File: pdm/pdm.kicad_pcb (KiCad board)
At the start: 4 copper layers, 129.5 x 91.4 mm, 111 parts, among them J1 Conn_01x04_Male, J2 Conn_01x12_Male, J3 Conn_01x08_Male, Q1 MMBT3904, Q10 Q_NPN_BCE, Q2 Q_NPN_BCE, Q3 MMBT3904, Q4 Q_NPN_BCE, Q5 MMBT3904, Q6 Q_NPN_BCE, Q7 MMBT3904, Q8 Q_NPN_BCE, Q9 MMBT3904, SW1 SW_Push, U1 AZ1117CH-3_3TRG1, U2 SN65HVD233, U3 STM32F042G6Ux, U4 BTS443P, U5 BTS443P, U6 BTS443P, U7 BTS443P, U8 BTS443P

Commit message: fixed issues #7 #8 #9 #10
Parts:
- removed 3V3_TP1, GND_TP1, Vin_TP1: TestPoint_Probe, TestPoint:TestPoint_Pad_D1.0mm
- removed C11: 22uF, Capacitor_SMD:CP_Elec_6.3x5.8
- removed G***: LOGO, pdm_v2:rarepepe
- added C1: 1uF, Capacitor_SMD:C_0805_2012Metric_Pad1.18x1.45mm_HandSolder, F.Cu at (158.3, 84.9)
- added J4: Conn_01x06_Female, Connector_PinHeader_2.54mm:PinHeader_1x06_P2.54mm_Vertical_SMD_Pin1Left, F.Cu at (176.4, 59.7)
- added M1: Fan, Connector_JST:JST_EH_B2B-EH-A_1x02_P2.50mm_Vertical, F.Cu at (218.1, 115.3)
- added M2: Fan, Connector_JST:JST_EH_B2B-EH-A_1x02_P2.50mm_Vertical, F.Cu at (218.1, 124.5)
- added Q11: Q_PMOS_DSG, Package_TO_SOT_SMD:TO-252-2, F.Cu at (153.8, 122.8)
- added R4: 120R, Capacitor_SMD:C_0805_2012Metric_Pad1.18x1.45mm_HandSolder, F.Cu at (208.2, 69.2)
- added TP9: TestPoint_Probe, TestPoint:TestPoint_Pad_D1.0mm, F.Cu at (118.7, 66.0)
- C10, C7, C8: moved to F.Cu
- C12, C13, C14, C15: value 10uF -> 1uF; footprint Capacitor_Tantalum_SMD:CP_EIA-3216-18_Kemet-A_Pad1.58x1.35mm_HandSolder -> Capacitor_SMD:C_0805_2012Metric_Pad1.18x1.45mm_HandSolder
- C16: value 10uF -> 0.1uF; footprint Capacitor_Tantalum_SMD:CP_EIA-3216-18_Kemet-A_Pad1.58x1.35mm_HandSolder -> Capacitor_SMD:C_0805_2012Metric_Pad1.18x1.45mm_HandSolder
- C3: value 0.1uF -> 0.1u
- C4, C5: value 20pF -> 16pF
- C6: value 10uF -> 10u
- H1, H2, H3, H4: footprint MountingHole:MountingHole_4mm_Pad_Via -> MountingHole:MountingHole_3mm_Pad_Via
- J3: value Conn_01x08_Male -> Conn_01x04_Female; footprint Connector_PinSocket_2.54mm:PinSocket_2x04_P2.54mm_Vertical_SMD -> Connector_PinHeader_2.54mm:PinHeader_1x04_P2.54mm_Vertical_SMD_Pin1Left
- Q1, Q3, Q5, Q7, Q9: value MMBT3904 -> BC817
- R1: value 600R -> 2k8
- R10, R17, R24, R31, R38: value 220R -> 680
- R14, R21, R28, R7: value 2k2 -> 2k8
- R15, R22, R29, R8: value 220R -> 10k
- R16, R23, R30, R37, R9: value 220R -> 1K5
- R3: value 600R -> 10k
- R35: value 2k2 -> 600R
- R36: value 220R -> 600R
- U1: value AZ1117CH-3_3TRG1 -> LM2937xS; footprint Package_TO_SOT_SMD:SOT-223 -> Package_TO_SOT_SMD:TO-263-3_TabPin2
- XTAL1: footprint Oscillator:Oscillator_SMD_Abracon_ASE-4Pin_3.2x2.5mm -> digikey-footprints:SMD-2_3.2x2.5mm
- moved C13 98.5 mm to (207.1, 85.3)
- moved R14 98.4 mm to (213.7, 79.1), turned to 90 degrees
- moved R15 98.0 mm to (207.1, 81.4), turned to 270 degrees
- moved R35 96.7 mm to (118.7, 61.5)
- moved C3 77.4 mm to (121.3, 67.1), turned to 270 degrees
- moved R36 75.8 mm to (134.0, 61.5), turned to 270 degrees
- moved Q3 74.2 mm to (186.4, 78.8)
- moved Q7 73.9 mm to (112.4, 78.5)
- moved Q9 73.5 mm to (137.0, 78.5)
- moved C16 61.5 mm to (149.1, 64.3), turned to 0 degrees
- moved R22 49.8 mm to (108.8, 80.8), turned to 270 degrees
- moved R29 49.7 mm to (133.5, 80.8), turned to 270 degrees
- moved C12 49.6 mm to (182.9, 85.1)
- moved R7 49.5 mm to (189.4, 78.9), turned to 90 degrees
- moved R21 49.3 mm to (115.4, 78.5), turned to 90 degrees
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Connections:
- C12 pad 1: /sense2 -> /sense4
- C13 pad 1: /sense1 -> /sense5
- C14 pad 1: /sense3 -> /sense1
- C15 pad 1: /sense4 -> /sense2
- C16 pad 1: /sense5 -> Net-(C16-Pad1)
- C3 pad 1: +3V3 -> +12V
- C6 pad 1: +12V -> +3V3
- D4 pad 1: /vout2 -> GND
- D5 pad 1: /vout1 -> GND
- D6 pad 1: /vout3 -> GND
- D7 pad 1: /vout4 -> GND
- D8 pad 1: /vout5 -> GND
- J1 pad 2: +12V -> /vin
- J1 pad 3: +12V -> /vin
- J1 pad 4: +12V -> /vin
- J2 pad 11: /_N -> /_P
- J2 pad 12: /_P -> /_N
- J2 pad 3: /vout1 -> /vout2
- J2 pad 4: /vout2 -> /vout3
- J2 pad 5: /vout3 -> /vout4
- J2 pad 6: /vout4 -> /vout5
- J2 pad 8: /vout3 -> /vout4
- J2 pad 9: /vout2 -> /vout3
- J3 pad 1: /_N -> GND
- J3 pad 2: /_P -> +3V3
- J3 pad 3: /NRST -> /_P
- J3 pad 4: /SWDIO -> /_N
- Q1 pad 1: /act2 -> Net-(Q1-Pad1)
- Q1 pad 2: Net-(Q1-Pad2) -> GND
- Q3 pad 1: /act1 -> Net-(Q3-Pad1)
- Q3 pad 2: Net-(Q3-Pad2) -> GND
- Q5 pad 1: /act3 -> Net-(Q5-Pad1)
- Q5 pad 2: Net-(Q5-Pad2) -> GND
- Q7 pad 1: /act4 -> Net-(Q7-Pad1)
- Q7 pad 2: Net-(Q7-Pad2) -> GND
- Q9 pad 1: /act5 -> Net-(Q9-Pad1)
- Q9 pad 2: Net-(Q9-Pad2) -> GND
- R1 pad 1: Net-(D1-Pad2) -> /act3
- R1 pad 2: +12V -> Net-(Q1-Pad1)
- R10 pad 1: Net-(Q1-Pad2) -> /vout2
- R14 pad 1: +3V3 -> /act5
- R14 pad 2: Net-(Q3-Pad3) -> Net-(Q5-Pad1)
- R15 pad 1: Net-(R15-Pad1) -> Net-(Q5-Pad3)
- R15 pad 2: Net-(Q3-Pad2) -> Net-(R15-Pad2)
- R17 pad 1: Net-(Q3-Pad2) -> /vout1
- R21 pad 1: +3V3 -> /act1
- R21 pad 2: Net-(Q5-Pad3) -> Net-(Q7-Pad1)
- R22 pad 1: Net-(R22-Pad1) -> Net-(Q7-Pad3)
- R22 pad 2: Net-(Q5-Pad2) -> Net-(R22-Pad2)
- R24 pad 1: Net-(Q5-Pad2) -> /vout3
- R28 pad 1: +3V3 -> /act2
- R28 pad 2: Net-(Q7-Pad3) -> Net-(Q9-Pad1)
- R29 pad 1: Net-(R29-Pad1) -> Net-(Q9-Pad3)
- R29 pad 2: Net-(Q7-Pad2) -> Net-(R29-Pad2)
- R3 pad 1: Net-(D2-Pad2) -> Net-(Q1-Pad3)
- R3 pad 2: +3V3 -> Net-(R3-Pad2)
- R31 pad 1: Net-(Q7-Pad2) -> /vout4
- R35 pad 1: +3V3 -> Net-(D1-Pad2)
- R35 pad 2: Net-(Q9-Pad3) -> +12V
- R36 pad 1: Net-(R36-Pad1) -> Net-(D2-Pad2)
- R36 pad 2: Net-(Q9-Pad2) -> +3V3
- R38 pad 1: Net-(Q9-Pad2) -> /vout5
- R5 pad 1: GND -> /DEBUG_BUTTON
- R5 pad 2: /DEBUG_BUTTON -> Net-(C16-Pad1)
- R7 pad 1: +3V3 -> /act4
- R7 pad 2: Net-(Q1-Pad3) -> Net-(Q3-Pad1)
- R8 pad 1: Net-(R8-Pad1) -> Net-(Q3-Pad3)
- R8 pad 2: Net-(Q1-Pad2) -> Net-(R8-Pad2)
- SW1 pad 1: /DEBUG_BUTTON -> Net-(C16-Pad1)
- U1 pad 1: GND -> +12V
- U1 pad 2: +3V3 -> GND
- U1 pad 3: +12V -> +3V3
- U3 pad 10: /sense5 -> /sense3
- U3 pad 11: /act1 -> /fuse1
- U3 pad 12: /act2 -> /act1
- U3 pad 13: /act3 -> /fuse2
- U3 pad 23: /act4 -> /act2
- U3 pad 24: /fuse1 -> /fuse3
- U3 pad 25: /fuse2 -> /act3
- U3 pad 26: /fuse3 -> /fuse4
- U3 pad 27: /fuse4 -> /act4
- U3 pad 6: /sense1 -> /sense4
- U3 pad 7: /sense2 -> /sense5
- U3 pad 8: /sense3 -> /sense1
- U3 pad 9: /sense4 -> /sense2
- U4 pad 2: Net-(R8-Pad1) -> Net-(R29-Pad2)
- U5 pad 2: Net-(R15-Pad1) -> Net-(R22-Pad2)
- U6 pad 2: Net-(R22-Pad1) -> Net-(R3-Pad2)
- U7 pad 2: Net-(R29-Pad1) -> Net-(R8-Pad2)
- U8 pad 2: Net-(R36-Pad1) -> Net-(R15-Pad2)
- XTAL1 pad 1: /OSC_N -> /OSC_P
- XTAL1 pad 2: /OSC_P -> /OSC_N
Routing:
- net /vout1: track 272.3 -> 103.6 mm
- net /vout2: track 212.2 -> 76.8 mm
- net +3V3: track 221.5 -> 104.7 mm, vias 21 -> 30
- net /vout5: track 140.8 -> 205.8 mm
- net +12V: track 55.6 -> 19.1 mm, vias 7 -> 202
- net /vout4: track 113.0 -> 148.9 mm
- net /cantx: track 13.2 -> 47.5 mm, vias 2 -> 4
- net /canrx: track 12.0 -> 45.5 mm, vias 2 -> 4
- net /NRST: track 52.5 -> 20.4 mm, vias 4 -> 2
- net Net-(Q1-Pad2): track 28.1 -> 0.00 mm, vias 2 -> 0
- net Net-(Q5-Pad2): track 28.1 -> 0.00 mm, vias 2 -> 0
- net Net-(Q9-Pad2): track 28.1 -> 0.00 mm, vias 2 -> 0
- net Net-(Q3-Pad2): track 28.1 -> 0.00 mm, vias 2 -> 0
- net Net-(Q7-Pad2): track 28.1 -> 0.00 mm, vias 2 -> 0
- net /fuse1: track 79.7 -> 106.9 mm
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- added copper zone on F.Cu, net +12V
- added copper zone on F.Cu, net +3V3
- added copper zone on F.Cu, net /vin
- added copper zone on F.Cu, net GND
- removed copper zone on In1.Cu, net +3V3
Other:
- board text added: "BLOCK 1"
- board text added: "BLOCK 2"
- board text added: "BLOCK 4 [HC]"
- board text added: "BLOCK 5 [HC]"
- board text added: "FAN1"
- board text added: "FAN2"
- board text added: "SWD"
- board text removed: "BLOCK 1 [HC]"
- board text removed: "BLOCK 2 [HC]"
- board text removed: "BLOCK 4"
- board text removed: "BLOCK 5"
- board text removed: "PROGRAMMING"

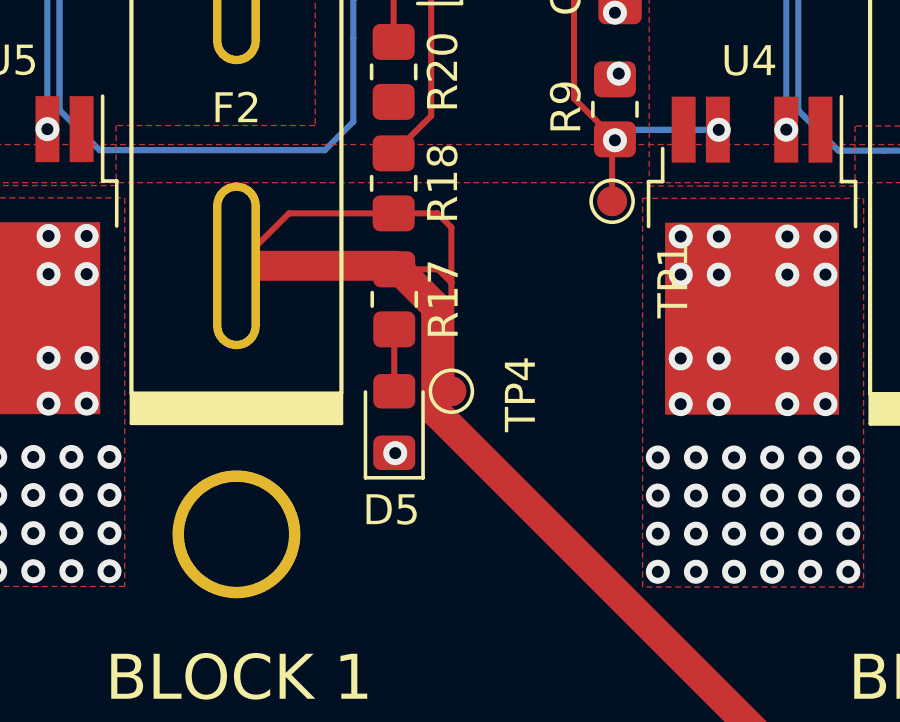
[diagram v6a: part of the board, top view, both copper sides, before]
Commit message: moved led's to side of mosfet for issue #9
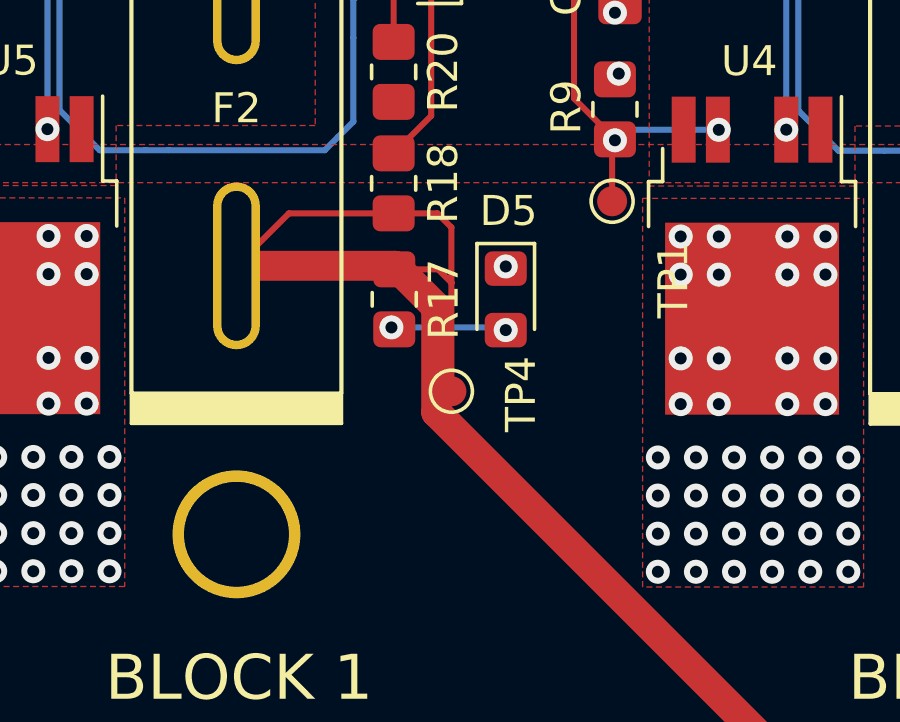
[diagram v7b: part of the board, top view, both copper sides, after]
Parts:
- moved D5 5.53 mm to (129.7, 95.6), turned to 270 degrees
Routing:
- net Net-(D5-Pad2): track 2.06 -> 3.97 mm, vias 0 -> 2
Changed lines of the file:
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@@
     (thickness 1.6)
     (drawings 118)
-    (tracks 1422)
+    (tracks 1426)
     (zones 0)
     (modules 113)
@@
   )
   (module LED_SMD:LED_0805_2012Metric_Pad1.15x1.40mm_HandSolder (layer F.Cu)
-    (at 125.951 99.673 90)
+    (at 129.667 95.584 270)
     (descr "LED SMD 0805 (2012 Metric), square (rectangular) end terminal, IPC_7351 nominal, (Body size source: https://docs.google.com/spreadsheets/d/1BsfQQcO9C6DZCsRaXUlFlo91Tg2WpOkGARC1WS5S8t0/edit?usp=sharing), generated with kicad-footprint-generator")
     (tags "LED handsolder")
@@
       (effects (font (size 0.5 0.5) (thickness 0.08)))
     )
-    (pad 2 smd roundrect (at 1.025 0 90) (size 1.15 1.4) (layers F.Cu F.Paste F.Mask) (roundrect_rratio 0.217391)
+    (pad 2 smd roundrect (at 1.025 0 270) (size 1.15 1.4) (layers F.Cu F.Paste F.Mask) (roundrect_rratio 0.217391)
       (net 41 "Net-(D5-Pad2)"))
-    (pad 1 smd roundrect (at -1.025 0 90) (size 1.15 1.4) (layers F.Cu F.Paste F.Mask) (roundrect_rratio 0.217391)
+    (pad 1 smd roundrect (at -1.025 0 270) (size 1.15 1.4) (layers F.Cu F.Paste F.Mask) (roundrect_rratio 0.217391)
       (net 1 GND))
     (model ${KISYS3DMOD}/LED_SMD.3dshapes/LED_0805_2012Metric.wrl
@@
   (segment (start 133.985 56.370001) (end 133.985 56.388) (width 1) (layer F.Cu) (net 1))
   (via (at 126.511 56.781) (size 0.8) (drill 0.4) (layers F.Cu B.Cu) (net 1))
-  (via (at 125.984 100.711) (size 0.8) (drill 0.4) (layers F.Cu B.Cu) (net 1))
-  (segment (start 125.971 100.698) (end 125.984 100.711) (width 0.2032) (layer F.Cu) (net 1))
-  (segment (start 125.951 100.698) (end 125.971 100.698) (width 0.2032) (layer F.Cu) (net 1))
   (via (at 111.379 77.47) (size 0.8) (drill 0.4) (layers F.Cu B.Cu) (net 1))
   (segment (start 111.395 77.486) (end 111.379 77.47) (width 0.2032) (layer F.Cu) (net 1))
@@
   (segment (start 151.517 127.006) (end 151.511 127) (width 1) (layer F.Cu) (net 1))
   (segment (start 151.517 127.009) (end 151.517 127.006) (width 1) (layer F.Cu) (net 1))
+  (via (at 129.667 94.488) (size 0.8) (drill 0.4) (layers F.Cu B.Cu) (net 1))
+  (segment (start 129.667 94.559) (end 129.667 94.488) (width 0.2032) (layer F.Cu) (net 1))
   (via (at 110.871 94.742) (size 0.8) (drill 0.4) (layers F.Cu B.Cu) (net 2))
   (via (at 112.141 94.742) (size 0.8) (drill 0.4) (layers F.Cu B.Cu) (net 2))
@@
   (segment (start 140.3985 56.499002) (end 140.3985 58.284) (width 0.2032) (layer F.Cu) (net 39))
   (segment (start 150.579 96.601) (end 150.578999 98.665) (width 0.2032) (layer F.Cu) (net 40))
-  (segment (start 125.951 96.584) (end 125.950999 98.648) (width 0.2032) (layer F.Cu) (net 41))
+  (via (at 125.857 96.52) (size 0.8) (drill 0.4) (layers F.Cu B.Cu) (net 41))
+  (segment (start 125.921 96.584) (end 125.857 96.52) (width 0.2032) (layer F.Cu) (net 41))
+  (segment (start 125.951 96.584) (end 125.921 96.584) (width 0.2032) (layer F.Cu) (net 41))
+  (segment (start 129.578 96.52) (end 129.667 96.609) (width 0.2032) (layer B.Cu) (net 41))
+  (via (at 129.667 96.609) (size 0.8) (drill 0.4) (layers F.Cu B.Cu) (net 41))
+  (segment (start 125.857 96.52) (end 129.578 96.52) (width 0.2032) (layer B.Cu) (net 41))
   (segment (start 161.529 79.946) (end 161.831 79.644) (width 0.2032) (layer F.Cu) (net 42))
   (segment (start 158.275 79.946) (end 161.529 79.946) (width 0.2032) (layer F.Cu) (net 42))

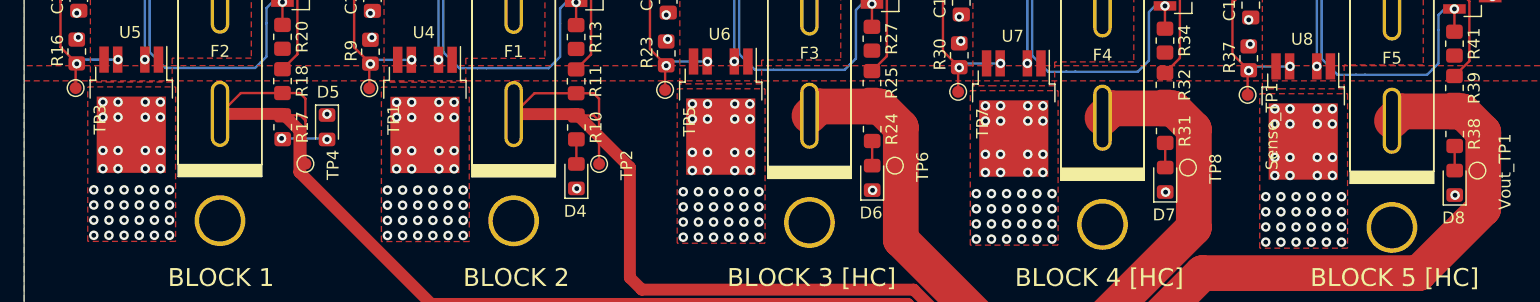
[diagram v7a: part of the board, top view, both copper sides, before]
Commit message: added more vias to LDR #10 & channged to pin female #8
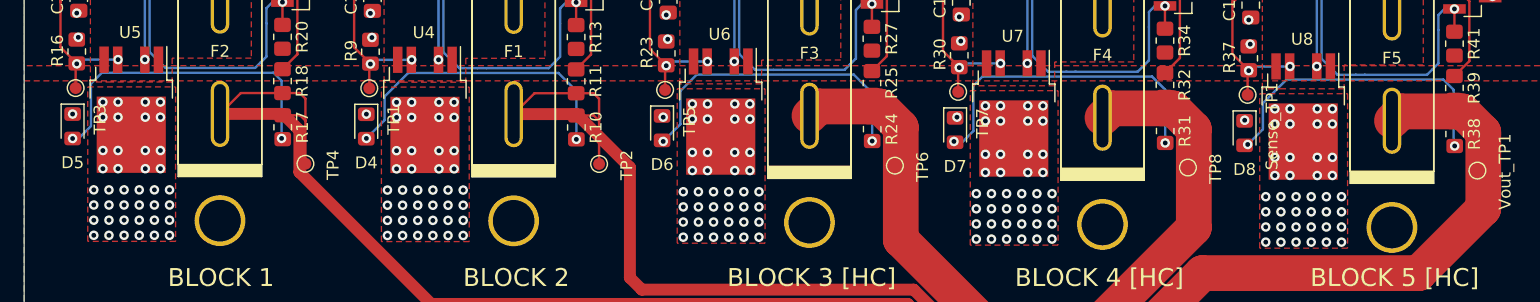
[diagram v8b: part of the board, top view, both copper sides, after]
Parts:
- moved D5 21.3 mm to (108.3, 95.5)
- moved D8 18.1 mm to (206.6, 96.1), turned to 270 degrees
- moved D4 18.1 mm to (133.0, 95.5), turned to 270 degrees
- moved D6 18.1 mm to (157.8, 95.7), turned to 270 degrees
- moved D7 18.1 mm to (182.3, 95.8), turned to 270 degrees
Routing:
- net Net-(D7-Pad2): track 2.06 -> 27.3 mm, vias 0 -> 2
- net Net-(D6-Pad2): track 2.06 -> 26.3 mm, vias 0 -> 2
- net Net-(D8-Pad2): track 2.06 -> 26.2 mm, vias 0 -> 2
- net Net-(D4-Pad2): track 2.06 -> 25.8 mm, vias 0 -> 2
- net Net-(D5-Pad2): track 3.97 -> 27.1 mm
